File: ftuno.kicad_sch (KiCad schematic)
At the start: 62 parts, among them CN1 AFC10-S04QCA-00, J1 Conn_01x08_Pin, J10 Conn_02x04_Odd_Even, J11 Conn_01x04_Socket, J2 Conn_01x08_Socket, J3 Conn_01x06_Pin, J4 Conn_01x06_Socket, J5 Conn_01x10_Pin, J6 Conn_01x10_Socket, J7 Conn_01x08_Pin, J8 Conn_01x08_Socket, J9 Conn_02x03_Odd_Even, Q1 AO3401, Q2 BSS138PS_C5224289, SW1 SK12D07VG4, SW2 TS-1187A-B-A-B, U1 ATmega328P-A, U2 CH340C, U3 SRV05-4, U4 TPS54302, U5 ME6217C33M5G, X1 CSTCE16M0V53-R0

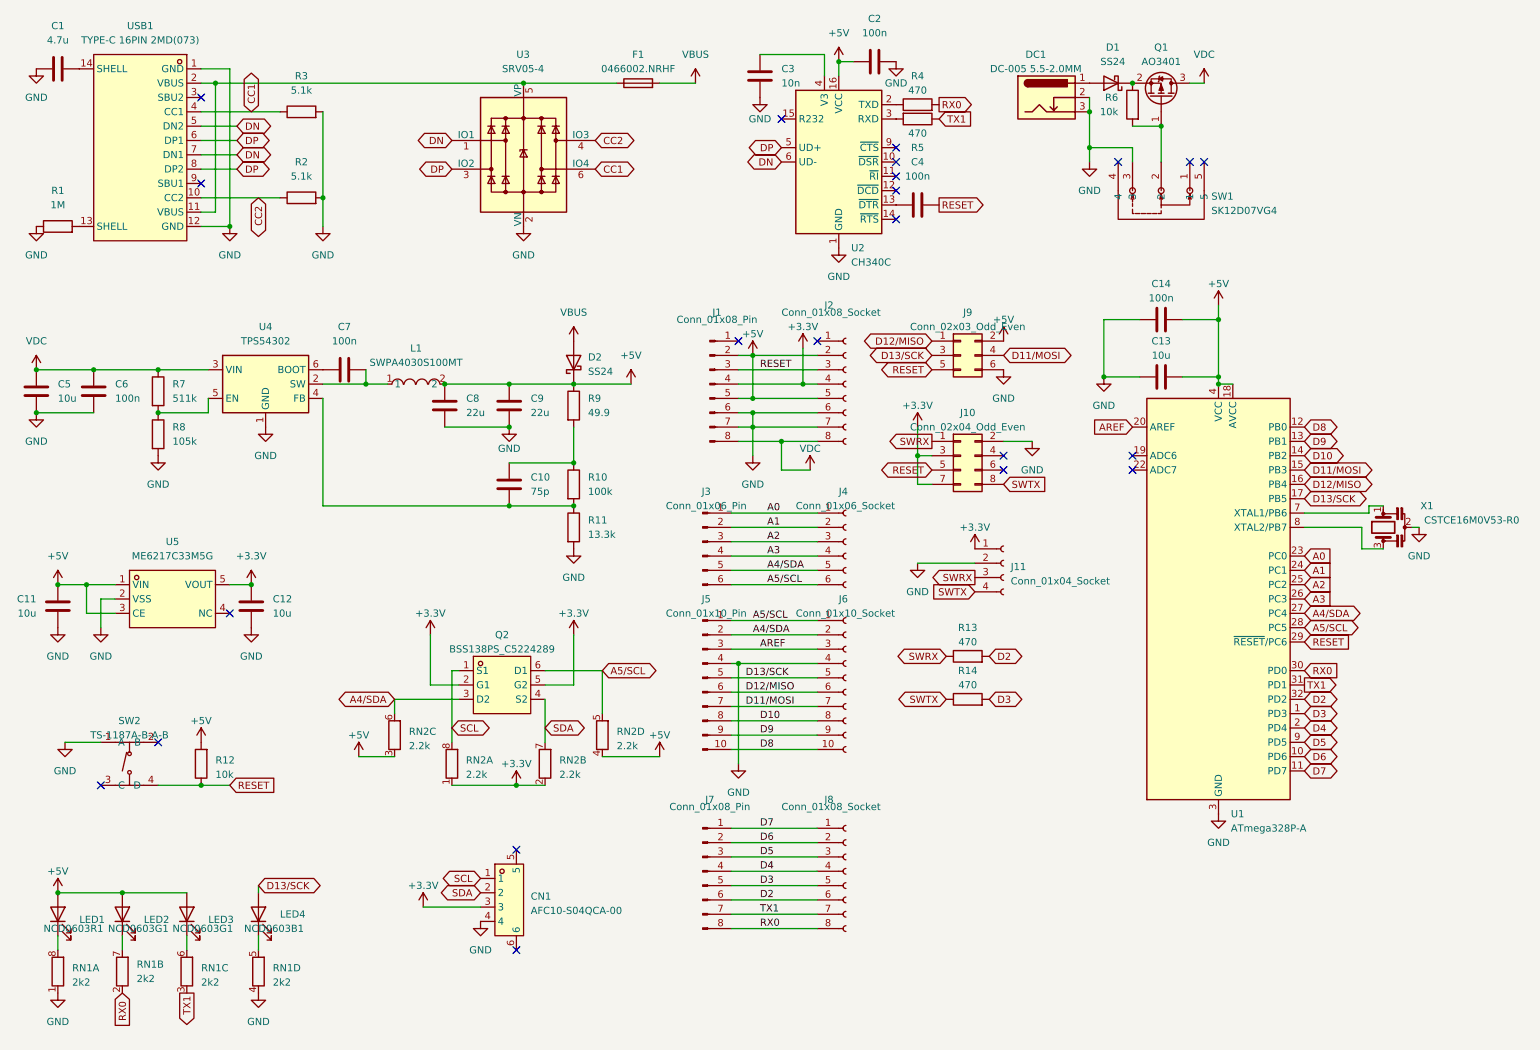
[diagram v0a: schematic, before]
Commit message: added UART level convertor, moved components, solved UART LED issue
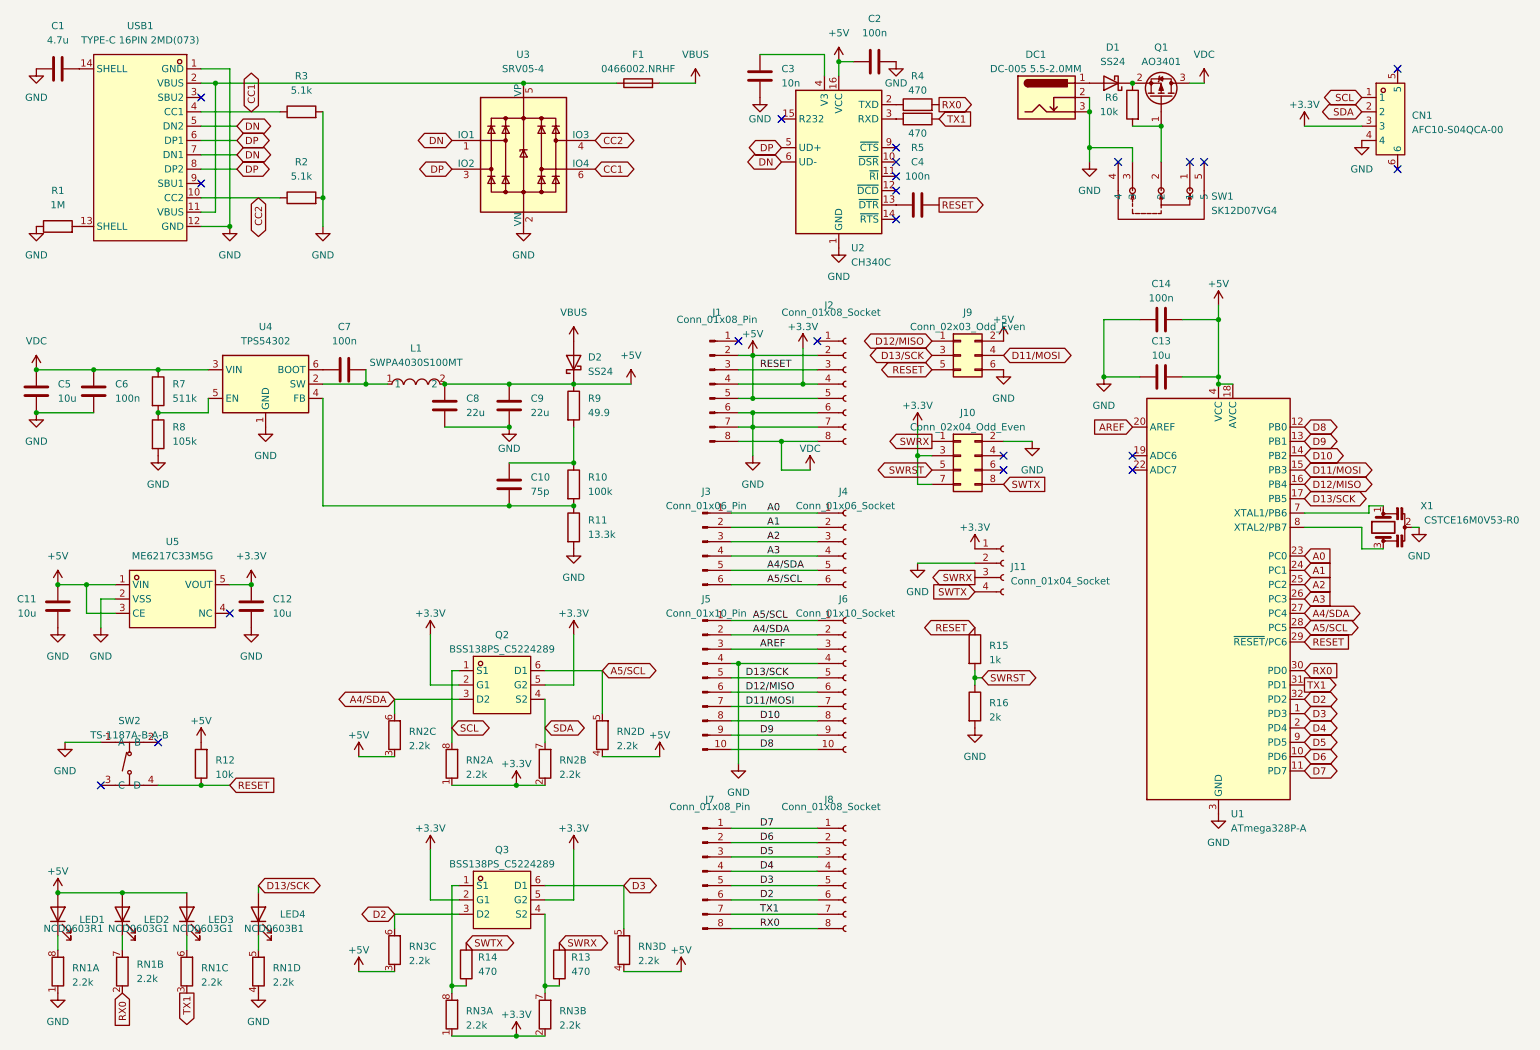
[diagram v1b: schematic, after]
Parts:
- added Q3: BSS138PS_C5224289, uno:SOT-363_L2.1-W1.3-P0.65-LS2.3-BL, symbol uno:BSS138PS_C5224289
- added R15: 1k, Resistor_SMD:R_0402_1005Metric, symbol Device:R
- added R16: 2k, Resistor_SMD:R_0402_1005Metric, symbol Device:R
- added RN3: 2.2k, Resistor_SMD:R_Array_Convex_4x0603, symbol Device:R_Pack04_Split
- RN1: value 2k2 -> 2.2k
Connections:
- net +3.3V: now also Q3.2 (G1), Q3.5 (G2), RN3.1 (R1.1), RN3.2 (R2.1)
- net +5V: now also RN3.3 (R3.1), RN3.4 (R4.1)
- net D2: now also Q3.3 (D2), RN3.6 (R3.2); no longer R13.2
- net D3: now also Q3.6 (D1), RN3.5 (R4.2); no longer R14.2
- net GND: now also R16.2
- net RESET: now also R15.1; no longer J10.5 (Pin_5)
- net SWRX: now also R13.2; no longer R13.1
- net SWTX: now also R14.2; no longer R14.1
- new net: Q3.1 (S1), R14.1, RN3.8 (R1.2)
- new net: Q3.4 (S2), R13.1, RN3.7 (R2.2)
- new net SWRST: J10.5 (Pin_5), R15.2, R16.1
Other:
- moved on the sheet: CN1

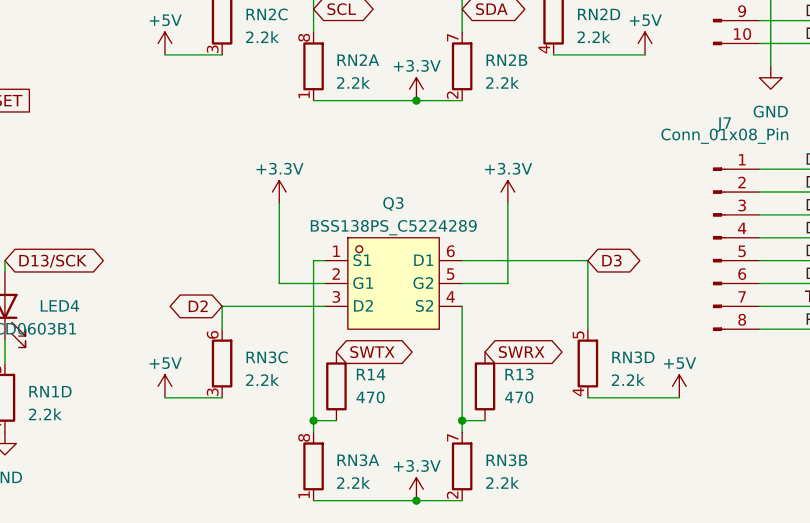
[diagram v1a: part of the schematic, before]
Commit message: change softwareserial pin to D7, D8
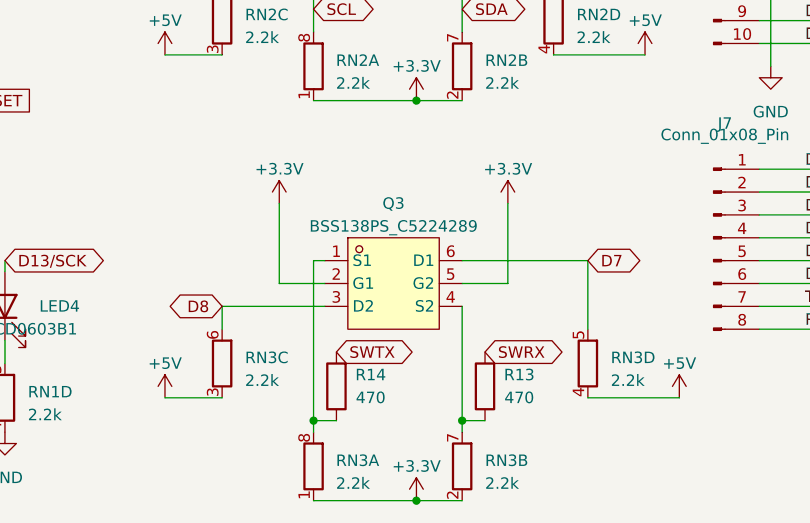
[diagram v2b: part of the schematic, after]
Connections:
- net D2: no longer Q3.3 (D2), RN3.6 (R3.2)
- net D3: no longer Q3.6 (D1), RN3.5 (R4.2)
- net D7: now also Q3.6 (D1), RN3.5 (R4.2)
- net D8: now also Q3.3 (D2), RN3.6 (R3.2)
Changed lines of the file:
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@@
     )
   )
-  (global_label "D3" (shape bidirectional) (at 123.19 167.64 0) (fields_autoplaced)
+  (global_label "D7" (shape bidirectional) (at 123.19 167.64 0) (fields_autoplaced)
     (effects (font (size 1.27 1.27)) (justify left))
     (property "Intersheetrefs" "${INTERSHEET_REFS}" (at 129.6866 167.64 0)
@@
     )
   )
-  (global_label "D2" (shape bidirectional) (at 82.55 172.72 180) (fields_autoplaced)
+  (global_label "D8" (shape bidirectional) (at 82.55 172.72 180) (fields_autoplaced)
     (effects (font (size 1.27 1.27)) (justify right))
     (property "Intersheetrefs" "${INTERSHEET_REFS}" (at 76.0534 172.72 0)

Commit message: use more common DC conn
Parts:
- DC1: value DC-005 5.5-2.0MM -> DC-005-20A; footprint uno:DC-IN-TH_DC-5520-1 -> uno:DC-IN-TH_DC-005-20A; LCSC Part C16214 -> C136744
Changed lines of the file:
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@@
       (effects (font (size 1.27 1.27)))
     )
-    (property "Value" "DC-005 5.5-2.0MM" (at 196.215 22.86 0)
+    (property "Value" "DC-005-20A " (at 196.215 22.86 0)
       (effects (font (size 1.27 1.27)))
     )
-    (property "Footprint" "uno:DC-IN-TH_DC-5520-1" (at 199.39 28.956 0)
+    (property "Footprint" "uno:DC-IN-TH_DC-005-20A" (at 199.39 28.956 0)
       (effects (font (size 1.27 1.27)) hide)
     )
@@
       (effects (font (size 1.27 1.27)) hide)
     )
-    (property "LCSC Part" "C16214" (at 198.12 43.18 0)
+    (property "LCSC Part" "C136744" (at 198.12 43.18 0)
       (effects (font (size 1.27 1.27)) hide)
     )

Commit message: fix qwiic
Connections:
- net +3.3V: now also CN1.2; no longer CN1.3
- net GND: now also CN1.1; no longer CN1.4
- net SCL: now also CN1.3; no longer CN1.1
- net SDA: now also CN1.4; no longer CN1.2

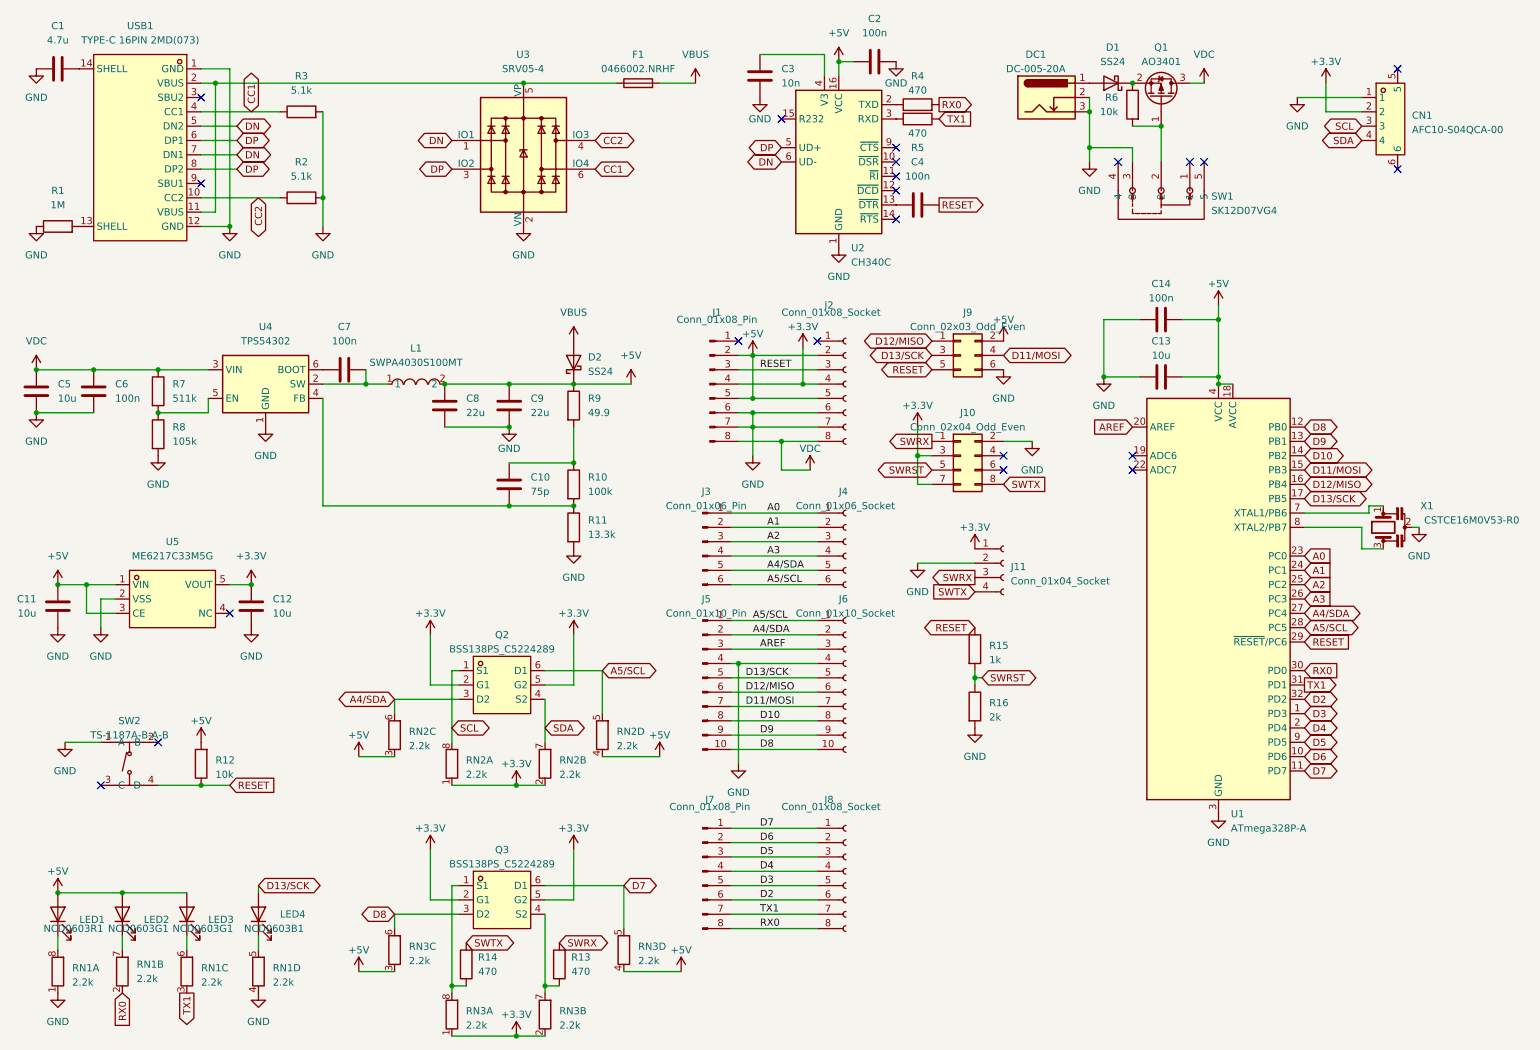
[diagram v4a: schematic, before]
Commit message: PCB update, replace USB conn, replace TVS, cleanup
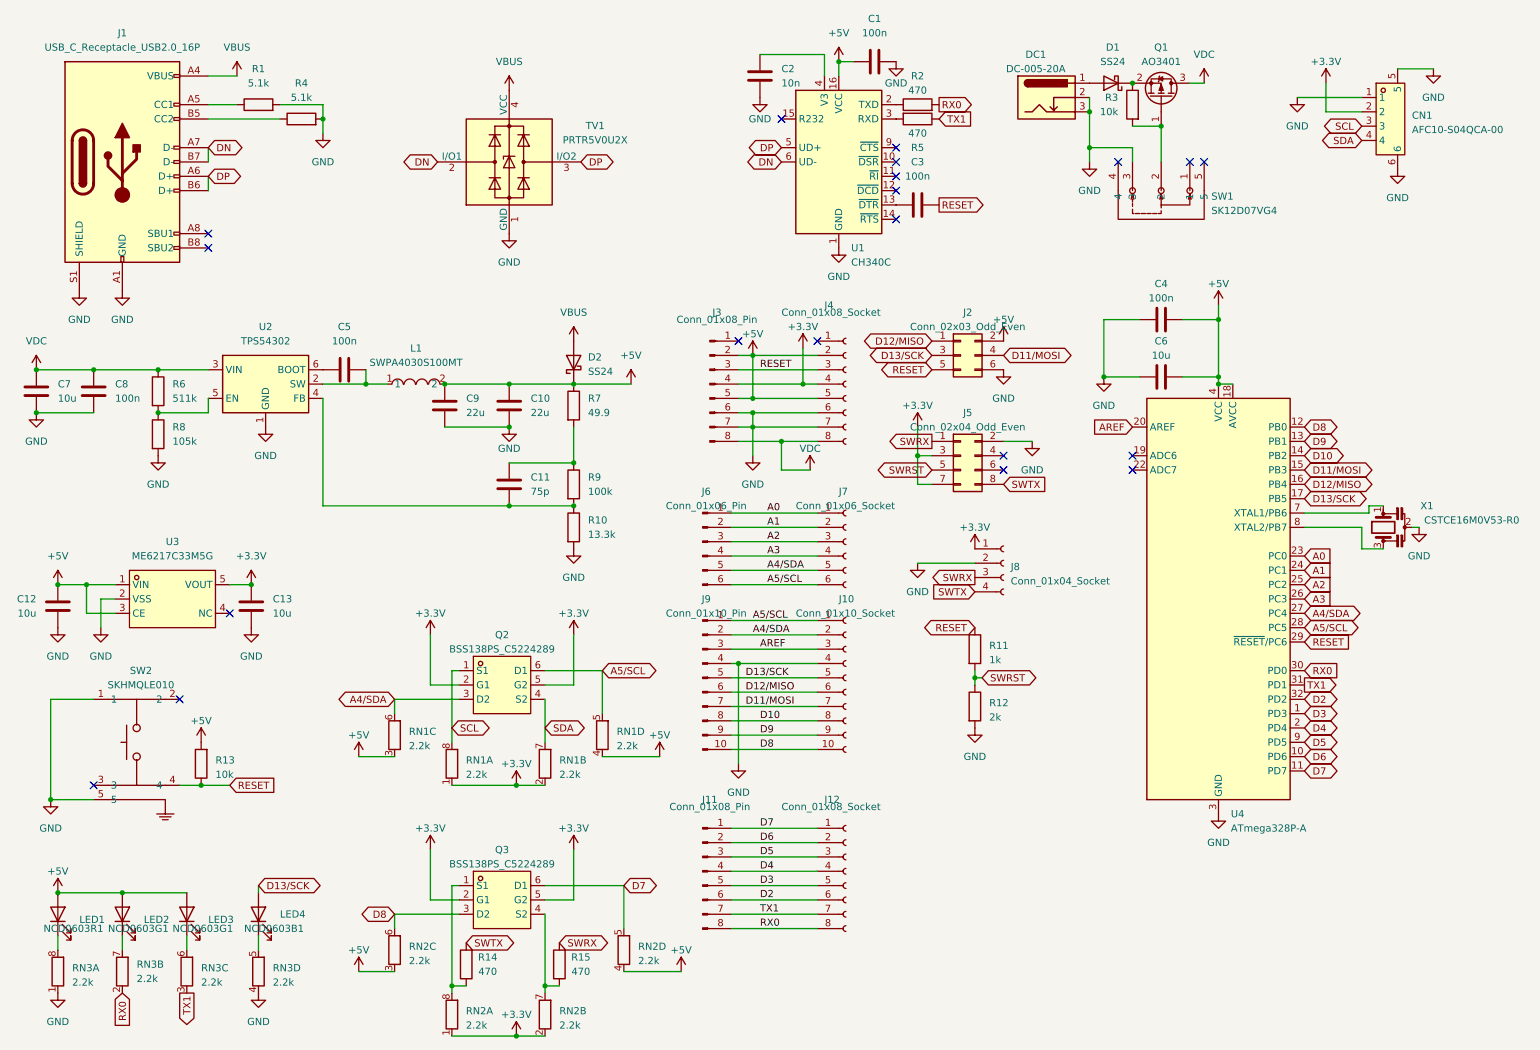
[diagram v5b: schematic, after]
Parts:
- removed C1: 4.7u, Capacitor_SMD:C_0603_1608Metric, symbol Device:C
- removed F1: 0466002.NRHF, Fuse:Fuse_1206_3216Metric, symbol Device:Fuse
- removed R2, R3: 5.1k, Resistor_SMD:R_0402_1005Metric, symbol Device:R
- removed SW2: TS-1187A-B-A-B, uno:SW-SMD_4P-L5.1-W5.1-P3.70-LS6.5-TL-2, symbol uno:TS-1187A-B-A-B
- removed U3: SRV05-4, Package_TO_SOT_SMD:SOT-23-6, symbol Power_Protection:SRV05-4
- removed USB1: TYPE-C 16PIN 2MD(073), uno:USB-C-SMD_TYPE-C-6PIN-2MD-073, symbol uno:TYPE-C16PIN2MD(073)
- added J1: USB_C_Receptacle_USB2.0_16P, Connector_USB:USB_C_Receptacle_G-Switch_GT-USB-7010ASV, symbol Connector:USB_C_Receptacle_USB2.0_16P
- added R4: 5.1k, Resistor_SMD:R_0402_1005Metric, symbol Device:R
- added SW2: SKHMQLE010, uno:KEY-SMD_4P-L6.2-W6.5-P4.50-LS8.0_SKHMXX, symbol uno:SKHMQLE010
- added TV1: PRTR5V0U2X, Package_TO_SOT_SMD:SOT-143, symbol Power_Protection:PRTR5V0U2X
- R1: value 1M -> 5.1k; footprint Resistor_SMD:R_0603_1608Metric -> Resistor_SMD:R_0402_1005Metric
- renumbered C2 to C1, C9 to C10, C10 to C11, C11 to C12, C12 to C13, C3 to C2, C4 to C3, C14 to C4, C7 to C5, C13 to C6, C5 to C7, C6 to C8, C8 to C9, J6 to J10, J7 to J11, J8 to J12, J9 to J2, J1 to J3, J2 to J4, J10 to J5, J3 to J6, J4 to J7, J11 to J8, J5 to J9, R11 to R10, R15 to R11, R16 to R12, R12 to R13, R13 to R15, R4 to R2, R6 to R3, R7 to R6, R9 to R7, R10 to R9, RN2 to RN1, RN3 to RN2, RN1 to RN3, U2 to U1, U4 to U2, U5 to U3, U1 to U4
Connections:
- net DN: now also J1.A7 (D-), J1.B7 (D-), TV1.2 (I/O1)
- net DP: now also J1.A6 (D+), J1.B6 (D+), TV1.3 (I/O2)
- net GND: now also CN1.5, CN1.6, R1.2, J1.A1 (GND), J1.A12 (GND), J1.B1 (GND), J1.B12 (GND), J1.S1 (SHIELD), R4.2, SW2.1, SW2.5, TV1.1 (GND); no longer R1.1
- net RESET: now also SW2.4
- net VBUS: now also J1.A4 (VBUS), J1.A9 (VBUS), J1.B4 (VBUS), J1.B9 (VBUS), TV1.4 (VCC)
- new net: J1.A5 (CC1), R1.1
- new net: J1.B5 (CC2), R4.1
- no-connect marks 22 -> 20
